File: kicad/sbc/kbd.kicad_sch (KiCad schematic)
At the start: 4 parts, among them IC1 ATMEGA8-P, P2 CONN_01X03, P3 ISP, P4 PS/2 Keyboard

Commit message: io area relayout
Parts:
- P3: footprint Connector_PinHeader_2.54mm:PinHeader_2x03_P2.54mm_Horizontal -> Connector_PinHeader_2.54mm:PinHeader_2x03_P2.54mm_Vertical
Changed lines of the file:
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@@
       (effects (font (size 1.27 1.27)))
     )
-    (property "Footprint" "Connector_PinHeader_2.54mm:PinHeader_2x03_P2.54mm_Horizontal" (at 167.64 97.79 0)
+    (property "Footprint" "Connector_PinHeader_2.54mm:PinHeader_2x03_P2.54mm_Vertical" (at 167.64 97.79 0)
       (effects (font (size 1.524 1.524)) hide)
     )

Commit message: routing
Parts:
- IC1: footprint Package_DIP:DIP-28_W7.62mm_LongPads -> Package_DIP:DIP-28_W7.62mm; symbol io-rescue:ATMEGA8-P -> MCU_Microchip_ATmega:ATmega8A-P
- P2: symbol io-rescue:CONN_01X03 -> Connector_Generic:Conn_01x03
- P3: symbol io-rescue:CONN_02X03 -> Connector_Generic:Conn_02x03_Odd_Even
- P4: symbol io-rescue:MINI_DIN_6 -> Connector:Mini-DIN-6
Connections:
- net GND: no longer P4.SH1 (PE1), P4.SH2 (PE2), P4.SH3 (PE3)
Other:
- moved on the sheet: IC1

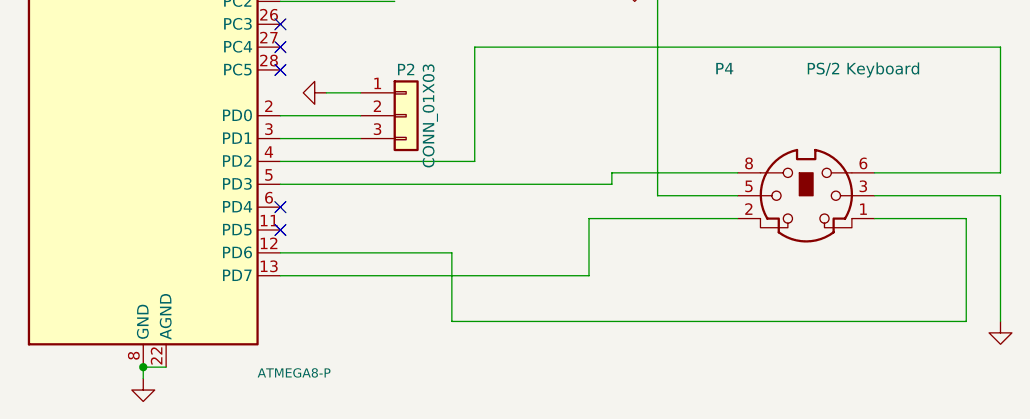
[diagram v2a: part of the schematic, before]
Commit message: regular sd socket separate masses for analog and digital cleanup routing
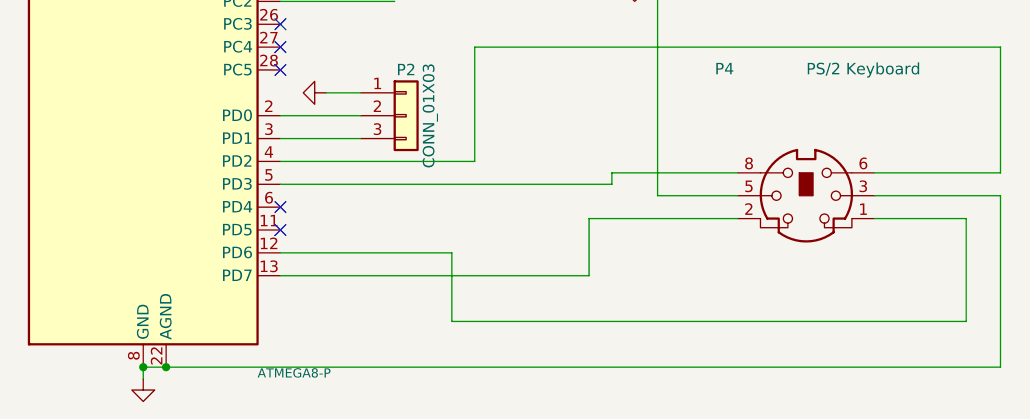
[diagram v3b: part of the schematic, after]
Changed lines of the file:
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@@
 (kicad_sch (version 20230121) (generator eeschema)
   (paper "A4")
+  (junction (at 125.73 118.11) (diameter 0) (color 0 0 0 0)
+  )
   (junction (at 123.19 36.83) (diameter 0) (color 0 0 0 0)
   )
@@
     (stroke (width 0) (type default))
   )
+  (wire (pts (xy 204.47 99.06) (xy 218.44 99.06))
+    (stroke (width 0) (type default))
+  )
   (wire (pts (xy 138.43 67.31) (xy 161.29 67.31))
     (stroke (width 0) (type default))
@@
     (stroke (width 0) (type default))
   )
-  (wire (pts (xy 218.44 99.06) (xy 218.44 113.03))
+  (wire (pts (xy 218.44 99.06) (xy 218.44 118.11))
     (stroke (width 0) (type default))
   )
@@
     (stroke (width 0) (type default))
   )
-  (wire (pts (xy 204.47 99.06) (xy 218.44 99.06))
-    (stroke (width 0) (type default))
-  )
   (wire (pts (xy 24.13 27.94) (xy 41.91 27.94))
     (stroke (width 0) (type default))
   )
+  (wire (pts (xy 138.43 92.71) (xy 147.32 92.71))
+    (stroke (width 0) (type default))
+  )
+  (wire (pts (xy 177.8 62.23) (xy 177.8 67.31))
+    (stroke (width 0) (type default))
+  )
+  (wire (pts (xy 173.99 67.31) (xy 177.8 67.31))
+    (stroke (width 0) (type default))
+  )
+  (wire (pts (xy 157.48 113.03) (xy 157.48 105.41))
+    (stroke (width 0) (type default))
+  )
+  (wire (pts (xy 91.44 36.83) (xy 123.19 36.83))
+    (stroke (width 0) (type default))
+  )
+  (wire (pts (xy 123.19 118.11) (xy 123.19 119.38))
+    (stroke (width 0) (type default))
+  )
+  (wire (pts (xy 180.34 64.77) (xy 173.99 64.77))
+    (stroke (width 0) (type default))
+  )
+  (wire (pts (xy 138.43 97.79) (xy 175.26 97.79))
+    (stroke (width 0) (type default))
+  )
+  (wire (pts (xy 123.19 118.11) (xy 125.73 118.11))
+    (stroke (width 0) (type default))
+  )
+  (wire (pts (xy 97.79 54.61) (xy 97.79 45.72))
+    (stroke (width 0) (type default))
+  )
+  (wire (pts (xy 123.19 36.83) (xy 123.19 46.99))
+    (stroke (width 0) (type default))
+  )
+  (wire (pts (xy 180.34 36.83) (xy 180.34 64.77))
+    (stroke (width 0) (type default))
+  )
+  (wire (pts (xy 218.44 118.11) (xy 125.73 118.11))
+    (stroke (width 0) (type default))
+  )
+  (wire (pts (xy 138.43 72.39) (xy 142.24 72.39))
+    (stroke (width 0) (type default))
+  )
+  (wire (pts (xy 138.43 77.47) (xy 151.13 77.47))
+    (stroke (width 0) (type default))
+  )
+  (wire (pts (xy 157.48 69.85) (xy 161.29 69.85))
+    (stroke (width 0) (type default))
+  )
+  (wire (pts (xy 161.29 60.96) (xy 161.29 64.77))
+    (stroke (width 0) (type default))
+  )
+  (wire (pts (xy 138.43 74.93) (xy 151.13 74.93))
+    (stroke (width 0) (type default))
+  )
+  (wire (pts (xy 138.43 107.95) (xy 172.72 107.95))
+    (stroke (width 0) (type default))
+  )
+  (wire (pts (xy 143.51 87.63) (xy 147.32 87.63))
+    (stroke (width 0) (type default))
+  )
+  (wire (pts (xy 175.26 96.52) (xy 189.23 96.52))
+    (stroke (width 0) (type default))
+  )
+  (wire (pts (xy 175.26 97.79) (xy 175.26 96.52))
+    (stroke (width 0) (type default))
+  )
+  (wire (pts (xy 157.48 45.72) (xy 157.48 69.85))
+    (stroke (width 0) (type default))
+  )
+  (wire (pts (xy 97.79 45.72) (xy 157.48 45.72))
+    (stroke (width 0) (type default))
+  )
+  (wire (pts (xy 160.02 95.25) (xy 160.02 82.55))
+    (stroke (width 0) (type default))
+  )
+  (wire (pts (xy 180.34 64.77) (xy 180.34 99.06))
+    (stroke (width 0) (type default))
+  )
+  (wire (pts (xy 172.72 101.6) (xy 189.23 101.6))
+    (stroke (width 0) (type default))
+  )
+  (wire (pts (xy 218.44 96.52) (xy 204.47 96.52))
+    (stroke (width 0) (type default))
+  )
   (wire (pts (xy 180.34 99.06) (xy 189.23 99.06))
-    (stroke (width 0) (type default))
-  )
-  (wire (pts (xy 138.43 92.71) (xy 147.32 92.71))
-    (stroke (width 0) (type default))
-  )
-  (wire (pts (xy 177.8 62.23) (xy 177.8 67.31))
-    (stroke (width 0) (type default))
-  )
-  (wire (pts (xy 173.99 67.31) (xy 177.8 67.31))
-    (stroke (width 0) (type default))
-  )
-  (wire (pts (xy 157.48 113.03) (xy 157.48 105.41))
-    (stroke (width 0) (type default))
-  )
-  (wire (pts (xy 91.44 36.83) (xy 123.19 36.83))
-    (stroke (width 0) (type default))
-  )
-  (wire (pts (xy 123.19 118.11) (xy 123.19 119.38))
-    (stroke (width 0) (type default))
-  )
-  (wire (pts (xy 180.34 64.77) (xy 173.99 64.77))
-    (stroke (width 0) (type default))
-  )
-  (wire (pts (xy 138.43 97.79) (xy 175.26 97.79))
-    (stroke (width 0) (type default))
-  )
-  (wire (pts (xy 123.19 118.11) (xy 125.73 118.11))
-    (stroke (width 0) (type default))
-  )
-  (wire (pts (xy 97.79 54.61) (xy 97.79 45.72))
-    (stroke (width 0) (type default))
-  )
-  (wire (pts (xy 123.19 36.83) (xy 123.19 46.99))
-    (stroke (width 0) (type default))
-  )
-  (wire (pts (xy 180.34 36.83) (xy 180.34 64.77))
-    (stroke (width 0) (type default))
-  )
-  (wire (pts (xy 138.43 72.39) (xy 142.24 72.39))
-    (stroke (width 0) (type default))
-  )
-  (wire (pts (xy 138.43 77.47) (xy 151.13 77.47))
-    (stroke (width 0) (type default))
-  )
-  (wire (pts (xy 157.48 69.85) (xy 161.29 69.85))
-    (stroke (width 0) (type default))
-  )
-  (wire (pts (xy 161.29 60.96) (xy 161.29 64.77))
-    (stroke (width 0) (type default))
-  )
-  (wire (pts (xy 138.43 74.93) (xy 151.13 74.93))
-    (stroke (width 0) (type default))
-  )
-  (wire (pts (xy 138.43 107.95) (xy 172.72 107.95))
-    (stroke (width 0) (type default))
-  )
-  (wire (pts (xy 143.51 87.63) (xy 147.32 87.63))
-    (stroke (width 0) (type default))
-  )
-  (wire (pts (xy 175.26 96.52) (xy 189.23 96.52))
-    (stroke (width 0) (type default))
-  )
-  (wire (pts (xy 175.26 97.79) (xy 175.26 96.52))
-    (stroke (width 0) (type default))
-  )
-  (wire (pts (xy 157.48 45.72) (xy 157.48 69.85))
-    (stroke (width 0) (type default))
-  )
-  (wire (pts (xy 97.79 45.72) (xy 157.48 45.72))
-    (stroke (width 0) (type default))
-  )
-  (wire (pts (xy 160.02 95.25) (xy 160.02 82.55))
-    (stroke (width 0) (type default))
-  )
-  (wire (pts (xy 180.34 64.77) (xy 180.34 99.06))
-    (stroke (width 0) (type default))
-  )
-  (wire (pts (xy 172.72 101.6) (xy 189.23 101.6))
-    (stroke (width 0) (type default))
-  )
-  (wire (pts (xy 218.44 96.52) (xy 204.47 96.52))
     (stroke (width 0) (type default))
   )
@@
         )
       )
-    )
-  )
-  (symbol (lib_id "power:GND") (at 218.44 113.03 0) (unit 1)
-    (in_bom yes) (on_board yes) (dnp no)
-    (property "Reference" "#PWR067" (at 218.44 113.03 0)
-      (effects (font (size 0.762 0.762)) hide)
-    )
-    (property "Value" "GND" (at 218.44 114.808 0)
-      (effects (font (size 0.762 0.762)) hide)
-    )
-    (property "Footprint" "" (at 218.44 113.03 0)
-      (effects (font (size 1.27 1.27)) hide)
-    )
-    (property "Datasheet" "" (at 218.44 113.03 0)
-      (effects (font (size 1.27 1.27)) hide)
-    )
-    (pin "1")
-    (instances
-      (project "sbc"
-        (path "/896d5dab-44ec-47d0-8232-7ef57773545e/ed21330b-597f-40ab-85f1-2b6eb55707bf"
-          (reference "#PWR067") (unit 1)
-        )
-      )
-      (project "io"
-        (path "/dd492dee-3ed3-48c7-8a89-2dc679fadc05/00000000-0000-0000-0000-000058e7e6c3"
-          (reference "#PWR042") (unit 1)
-        )
-      )

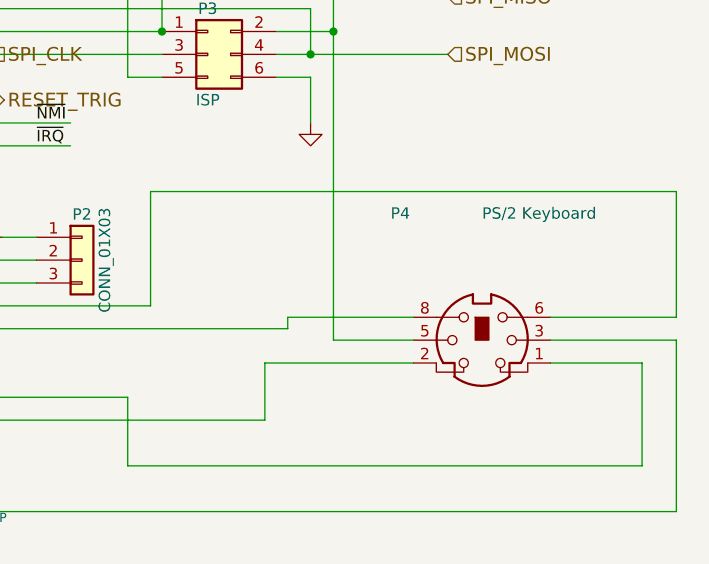
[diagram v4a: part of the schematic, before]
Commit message: new ps/2 mini din footprint
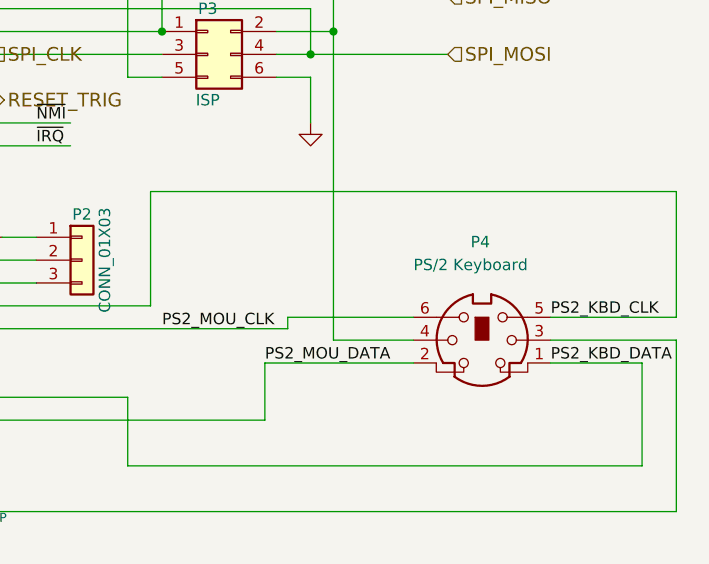
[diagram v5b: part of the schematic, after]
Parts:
- P4: footprint DIN:mini_din-M_DIN6 -> minidin:Mini_DIN_6_TE_Connectivity
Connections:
- net VCC: now also P4.4; no longer P4.5
- net PS2_KBD_DATA: now reaches IC1.12 (PD6), P4.1
- net PS2_MOU_DATA: now reaches IC1.13 (PD7), P4.2
- net PS2_KBD_CLK: now reaches IC1.4 (PD2)
- net PS2_KBD_CLK: now also P4.5; no longer P4.6
- net PS2_MOU_CLK: now reaches IC1.5 (PD3)
- net PS2_MOU_CLK: now also P4.6; no longer P4.8
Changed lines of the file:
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@@
+    (effects (font (size 1.27 1.27)) (justify left bottom))
+  )
+  (label "PS2_MOU_CLK" (at 161.29 97.79 0) (fields_autoplaced)
+    (effects (font (size 1.27 1.27)) (justify left bottom))
+  )
+  (label "PS2_MOU_DATA" (at 172.72 101.6 0) (fields_autoplaced)
     (effects (font (size 1.27 1.27)) (justify left bottom))
   )
   (label "~{RESET}" (at 99.06 54.61 0) (fields_autoplaced)
+    (effects (font (size 1.27 1.27)) (justify left bottom))
+  )
+  (label "PS2_KBD_CLK" (at 204.47 96.52 0) (fields_autoplaced)
+    (effects (font (size 1.27 1.27)) (justify left bottom))
+  )
+  (label "PS2_KBD_DATA" (at 204.47 101.6 0) (fields_autoplaced)
     (effects (font (size 1.27 1.27)) (justify left bottom))
   )
@@
   (symbol (lib_id "Connector:Mini-DIN-6") (at 196.85 99.06 0) (unit 1)
     (in_bom yes) (on_board yes) (dnp no)
-    (property "Reference" "P4" (at 186.69 85.725 0)
+    (property "Reference" "P4" (at 195.58 88.9 0)
       (effects (font (size 1.27 1.27)) (justify left bottom))
     )
-    (property "Value" "PS/2 Keyboard" (at 196.85 85.725 0)
+    (property "Value" "PS/2 Keyboard" (at 189.23 91.44 0)
       (effects (font (size 1.27 1.27)) (justify left bottom))
     )
-    (property "Footprint" "DIN:mini_din-M_DIN6" (at 196.85 99.06 0)
+    (property "Footprint" "minidin:Mini_DIN_6_TE_Connectivity" (at 196.85 99.06 0)
       (effects (font (size 1.27 1.27)) hide)
     )
@@
     (pin "2")
     (pin "3")
+    (pin "4")
     (pin "5")
     (pin "6")
-    (pin "8")
     (instances
       (project "sbc"

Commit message: moved all symbols into custom library
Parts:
- IC1: symbol MCU_Microchip_ATmega:ATmega8A-P -> steckschwein:ATmega8A-P
- P2: symbol Connector_Generic:Conn_01x03 -> steckschwein:Conn_01x03
- P3: symbol Connector_Generic:Conn_02x03_Odd_Even -> steckschwein:Conn_02x03_Odd_Even
- P4: symbol Connector:Mini-DIN-6 -> steckschwein:Mini-DIN-6
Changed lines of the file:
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@@
     (effects (font (size 1.524 1.524)) (justify left))
   )
-  (symbol (lib_id "Connector:Mini-DIN-6") (at 196.85 99.06 0) (unit 1)
+  (symbol (lib_id "steckschwein:Mini-DIN-6") (at 196.85 99.06 0) (unit 1)
     (in_bom yes) (on_board yes) (dnp no)
     (property "Reference" "P4" (at 195.58 88.9 0)
@@
     )
   )
-  (symbol (lib_id "Connector_Generic:Conn_01x03") (at 152.4 90.17 0) (unit 1)
+  (symbol (lib_id "steckschwein:Conn_01x03") (at 152.4 90.17 0) (unit 1)
     (in_bom yes) (on_board yes) (dnp no)
     (property "Reference" "P2" (at 152.4 85.09 0)
@@
     )
   )
-  (symbol (lib_id "Connector_Generic:Conn_02x03_Odd_Even") (at 166.37 67.31 0) (unit 1)
+  (symbol (lib_id "steckschwein:Conn_02x03_Odd_Even") (at 166.37 67.31 0) (unit 1)
     (in_bom yes) (on_board yes) (dnp no)
     (property "Reference" "P3" (at 166.37 62.23 0)
@@
     )
   )
-  (symbol (lib_id "MCU_Microchip_ATmega:ATmega8A-P") (at 123.19 82.55 0) (unit 1)
+  (symbol (lib_id "steckschwein:ATmega8A-P") (at 123.19 82.55 0) (unit 1)
     (in_bom yes) (on_board yes) (dnp no)
     (property "Reference" "IC1" (at 104.14 49.53 0)

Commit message: moved all footprints into local library
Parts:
- IC1: footprint Package_DIP:DIP-28_W7.62mm -> steckschwein:DIP-28_W7.62mm_LongPads
- P2: footprint Connector_PinHeader_2.54mm:PinHeader_1x03_P2.54mm_Vertical -> steckschwein:PinHeader_1x03_P2.54mm_Vertical
- P3: footprint Connector_PinHeader_2.54mm:PinHeader_2x03_P2.54mm_Vertical -> steckschwein:PinHeader_2x03_P2.54mm_Vertical
- P4: footprint minidin:Mini_DIN_6_TE_Connectivity -> steckschwein:Mini_DIN_6_TE_Connectivity
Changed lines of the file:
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@@
       (effects (font (size 1.27 1.27)) (justify left bottom))
     )
-    (property "Footprint" "minidin:Mini_DIN_6_TE_Connectivity" (at 196.85 99.06 0)
+    (property "Footprint" "steckschwein:Mini_DIN_6_TE_Connectivity" (at 196.85 99.06 0)
       (effects (font (size 1.27 1.27)) hide)
     )
@@
       (effects (font (size 1.27 1.27)))
     )
-    (property "Footprint" "Connector_PinHeader_2.54mm:PinHeader_1x03_P2.54mm_Vertical" (at 152.4 90.17 0)
+    (property "Footprint" "steckschwein:PinHeader_1x03_P2.54mm_Vertical" (at 152.4 90.17 0)
       (effects (font (size 1.27 1.27)) hide)
     )
@@
       (effects (font (size 1.27 1.27)))
     )
-    (property "Footprint" "Connector_PinHeader_2.54mm:PinHeader_2x03_P2.54mm_Vertical" (at 166.37 67.31 0)
+    (property "Footprint" "steckschwein:PinHeader_2x03_P2.54mm_Vertical" (at 166.37 67.31 0)
       (effects (font (size 1.27 1.27)) hide)
     )
@@
       (effects (font (size 1.016 1.016)) (justify left bottom))
     )
-    (property "Footprint" "Package_DIP:DIP-28_W7.62mm" (at 123.19 82.55 0)
+    (property "Footprint" "steckschwein:DIP-28_W7.62mm_LongPads" (at 123.19 82.55 0)
       (effects (font (size 1.27 1.27) italic) hide)
     )
